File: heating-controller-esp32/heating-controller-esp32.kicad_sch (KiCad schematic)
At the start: 25 parts, among them J3 76829-0104, J4 76829-0104, J5 76829-0104, J6 76829-0104, J7 76829-0104, J8 76829-0104, J9 76829-0104

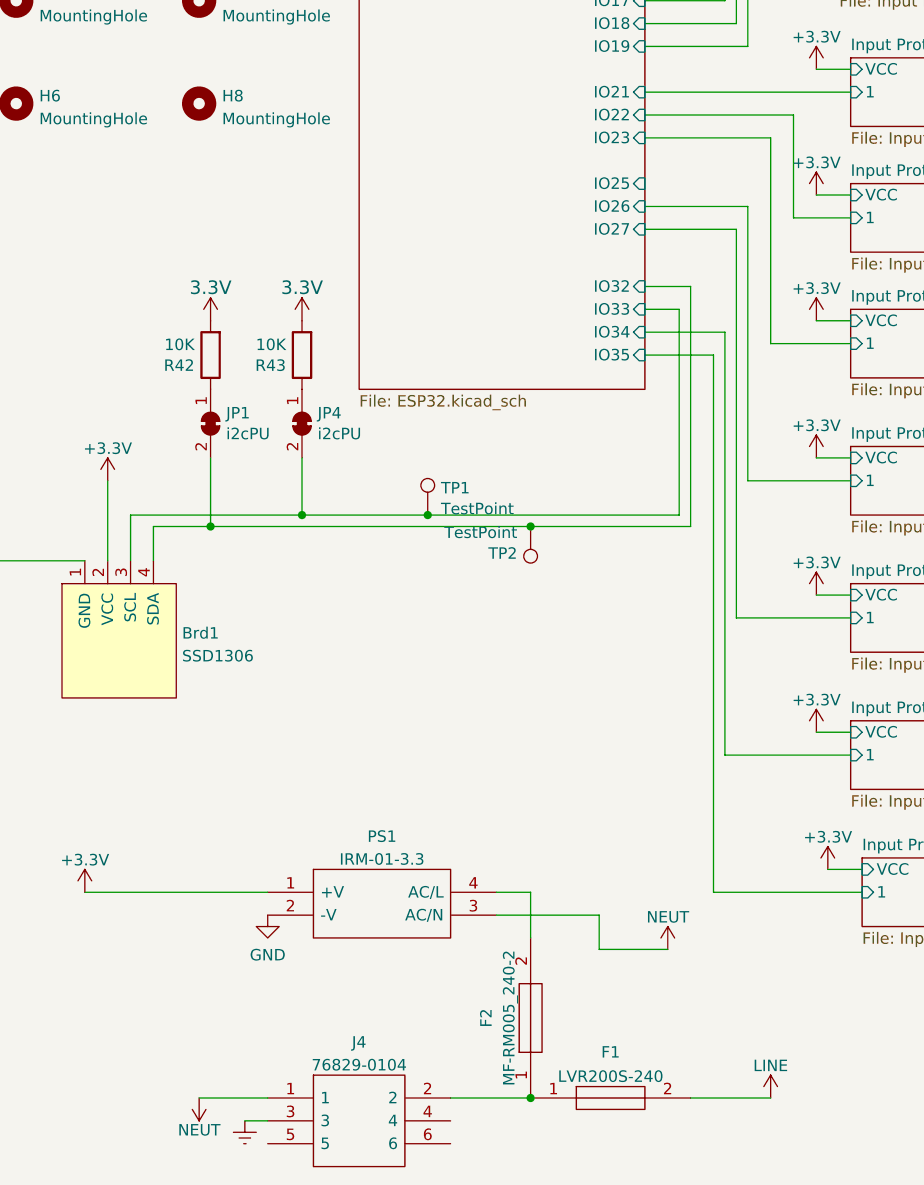
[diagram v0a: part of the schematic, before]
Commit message: Assign netclasses (should have done this earlier)! Small tweaks; status LED added.
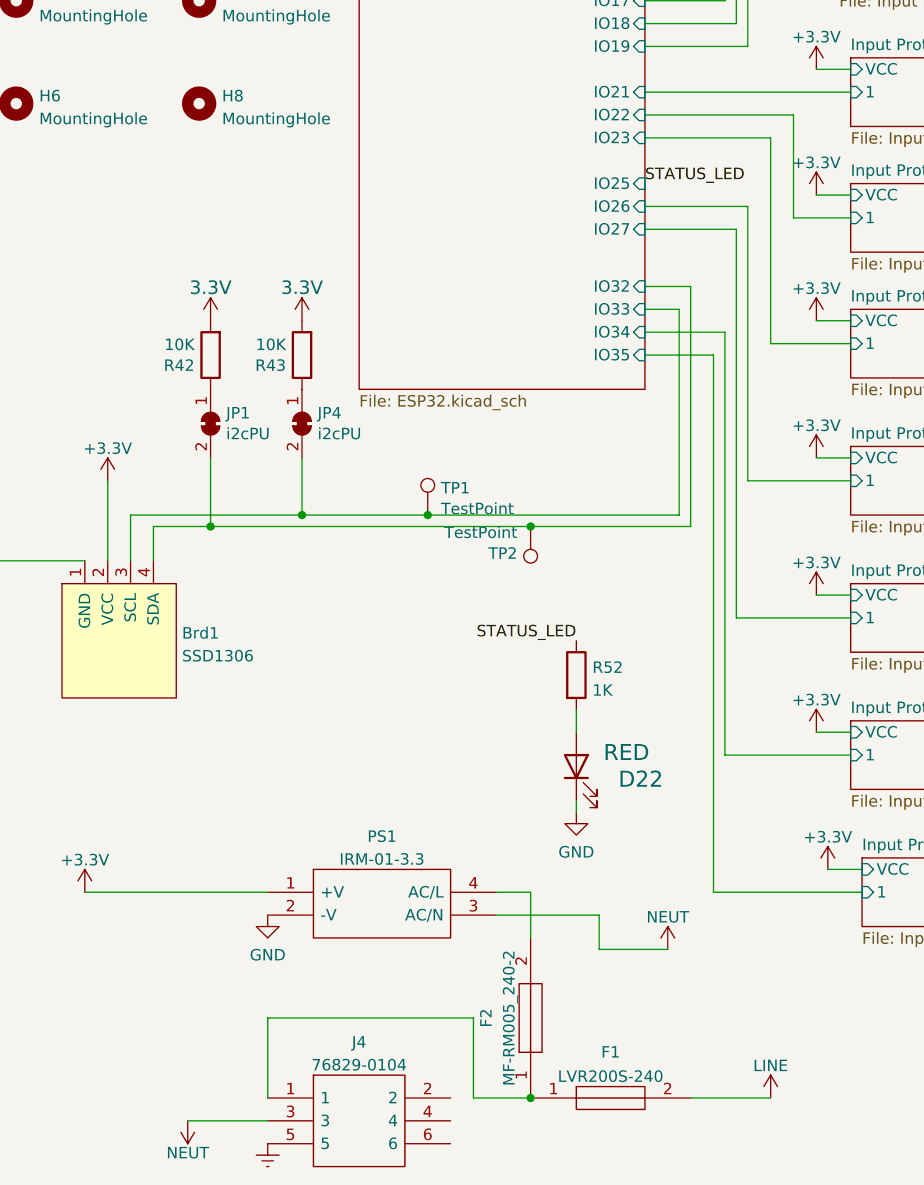
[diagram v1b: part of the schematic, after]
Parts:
- added D22: RED, LED_SMD:LED_0603_1608Metric, symbol Device:LED
- added R52: 1K, Resistor_SMD:R_0603_1608Metric, symbol Device:R
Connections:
- net Earth: now also J4.5; no longer J4.3
- net GND: now also D22.1 (K)
- net NEUT: now also J4.3; no longer J4.1
- net at F1.1, F2.1: now also J4.1; no longer J4.2
- new net: D22.2 (A), R52.2
- new net STATUS_LED: R52.1
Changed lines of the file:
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@@
   (junction (at 77.47 172.72) (diameter 0) (color 0 0 0 0)
   )
-  (wire (pts (xy 68.58 172.72) (xy 77.47 172.72))
-    (stroke (width 0) (type default) (color 0 0 0 0))
-  )
   (wire (pts (xy 100.33 53.34) (xy 100.33 30.48))
     (stroke (width 0) (type default) (color 0 0 0 0))
@@
     (stroke (width 0) (type default) (color 0 0 0 0))
   )
+  (wire (pts (xy 77.47 172.72) (xy 71.12 172.72))
+    (stroke (width 0) (type default) (color 0 0 0 0))
+  )
   (wire (pts (xy 190.5 88.9) (xy 204.47 88.9))
     (stroke (width 0) (type default) (color 0 0 0 0))
@@
     (stroke (width 0) (type default) (color 0 0 0 0))
   )
+  (wire (pts (xy 71.12 163.83) (xy 48.26 163.83))
+    (stroke (width 0) (type default) (color 0 0 0 0))
+  )
   (wire (pts (xy 93.98 15.24) (xy 93.98 40.64))
     (stroke (width 0) (type default) (color 0 0 0 0))
@@
     (stroke (width 0) (type default) (color 0 0 0 0))
   )
-  (wire (pts (xy 48.26 172.72) (xy 40.64 172.72))
-    (stroke (width 0) (type default) (color 0 0 0 0))
-  )
   (wire (pts (xy 100.33 119.38) (xy 113.03 119.38))
     (stroke (width 0) (type default) (color 0 0 0 0))
@@
     (stroke (width 0) (type default) (color 0 0 0 0))
   )
-  (wire (pts (xy 45.72 175.26) (xy 48.26 175.26))
-    (stroke (width 0) (type default) (color 0 0 0 0))
-  )
   (wire (pts (xy 101.6 73.66) (xy 90.17 73.66))
     (stroke (width 0) (type default) (color 0 0 0 0))
@@
     (stroke (width 0) (type default) (color 0 0 0 0))
   )
+  (wire (pts (xy 82.55 139.7) (xy 82.55 140.97))
+    (stroke (width 0) (type default) (color 0 0 0 0))
+  )
   (wire (pts (xy 90.17 45.72) (xy 96.52 45.72))
     (stroke (width 0) (type default) (color 0 0 0 0))
@@
     (stroke (width 0) (type default) (color 0 0 0 0))
   )
+  (wire (pts (xy 82.55 129.54) (xy 82.55 132.08))
+    (stroke (width 0) (type default) (color 0 0 0 0))
+  )
   (wire (pts (xy 101.6 104.14) (xy 101.6 73.66))
     (stroke (width 0) (type default) (color 0 0 0 0))
@@
     (stroke (width 0) (type default) (color 0 0 0 0))
   )
+  (wire (pts (xy 71.12 172.72) (xy 71.12 163.83))
+    (stroke (width 0) (type default) (color 0 0 0 0))
+  )
   (wire (pts (xy 77.47 109.22) (xy 41.91 109.22))
     (stroke (width 0) (type default) (color 0 0 0 0))
@@
     (stroke (width 0) (type default) (color 0 0 0 0))
   )
+  (wire (pts (xy 48.26 163.83) (xy 48.26 172.72))
+    (stroke (width 0) (type default) (color 0 0 0 0))
+  )
   (wire (pts (xy 95.25 109.22) (xy 77.47 109.22))
     (stroke (width 0) (type default) (color 0 0 0 0))
@@
   )
   (wire (pts (xy 85.09 152.4) (xy 85.09 156.21))
+    (stroke (width 0) (type default) (color 0 0 0 0))
+  )
+  (wire (pts (xy 39.37 175.26) (xy 48.26 175.26))
     (stroke (width 0) (type default) (color 0 0 0 0))
   )
@@
     (effects (font (size 1.27 1.27)) (justify left bottom))
   )
+  (label "STATUS_LED" (at 90.17 71.12 0)
+    (effects (font (size 1.27 1.27)) (justify left bottom))
+  )
   (label "Valve_Microswitch_4" (at 137.16 119.38 0)
     (effects (font (size 1.27 1.27)) (justify left bottom))
@@
   (label "Valve_Microswitch_2" (at 226.06 52.07 0)
     (effects (font (size 1.27 1.27)) (justify left bottom))
+  )
+  (label "STATUS_LED" (at 82.55 121.92 180)
+    (effects (font (size 1.27 1.27)) (justify right bottom))
   )
   (label "DHW_Thermostat" (at 232.41 142.24 0)
@@
     (pin "2")
   )
+  (symbol (lib_id "power:GND") (at 82.55 140.97 0) (unit 1)
+    (in_bom yes) (on_board yes) (fields_autoplaced)
+    (property "Reference" "#PWR0192" (id 0) (at 82.55 147.32 0)
+      (effects (font (size 1.27 1.27)) hide)
+    )
+    (property "Value" "GND" (id 1) (at 82.55 145.4134 0))
+    (property "Footprint" "" (id 2) (at 82.55 140.97 0)
+      (effects (font (size 1.27 1.27)) hide)
+    )
+    (property "Datasheet" "" (id 3) (at 82.55 140.97 0)
+      (effects (font (size 1.27 1.27)) hide)
+    )
+    (pin "1")
+  )
   (symbol (lib_id "power:+3.3V") (at 107.95 27.94 0) (unit 1)
     (in_bom yes) (on_board yes) (fields_autoplaced)
@@
     (pin "6")
   )
-  (symbol (lib_id "power:NEUT") (at 40.64 172.72 180) (unit 1)
-    (in_bom yes) (on_board yes) (fields_autoplaced)
-    (property "Reference" "#PWR0115" (id 0) (at 40.64 168.91 0)
-      (effects (font (size 1.27 1.27)) hide)
-    )
-    (property "Value" "NEUT" (id 1) (at 40.64 176.2958 0))
-    (property "Footprint" "" (id 2) (at 40.64 172.72 0)
-      (effects (font (size 1.27 1.27)) hide)
-    )
-    (property "Datasheet" "" (id 3) (at 40.64 172.72 0)
+  (symbol (lib_id "Device:R") (at 82.55 125.73 0) (unit 1)
+    (in_bom yes) (on_board yes) (fields_autoplaced)
+    (property "Reference" "R52" (id 0) (at 84.328 124.8953 0)
+      (effects (font (size 1.27 1.27)) (justify left))
+    )
+    (property "Value" "1K" (id 1) (at 84.328 127.4322 0)
+      (effects (font (size 1.27 1.27)) (justify left))
+    )
+    (property "Footprint" "Resistor_SMD:R_0603_1608Metric" (id 2) (at 80.772 125.73 90)
+      (effects (font (size 1.27 1.27)) hide)
+    )
+    (property "Datasheet" "~" (id 3) (at 82.55 125.73 0)
+      (effects (font (size 1.27 1.27)) hide)
+    )
+    (property "LCSC" "C21190" (id 4) (at 82.55 125.73 0)
+      (effects (font (size 1.27 1.27)) hide)
+    )
+    (pin "1")
+    (pin "2")
+  )
+  (symbol (lib_id "power:NEUT") (at 39.37 175.26 180) (unit 1)
+    (in_bom yes) (on_board yes) (fields_autoplaced)
+    (property "Reference" "#PWR0115" (id 0) (at 39.37 171.45 0)
+      (effects (font (size 1.27 1.27)) hide)
+    )
+    (property "Value" "NEUT" (id 1) (at 39.37 178.8358 0))
+    (property "Footprint" "" (id 2) (at 39.37 175.26 0)
+      (effects (font (size 1.27 1.27)) hide)
+    )
+    (property "Datasheet" "" (id 3) (at 39.37 175.26 0)
       (effects (font (size 1.27 1.27)) hide)
     )
@@
     (pin "6")
   )
-  (symbol (lib_id "power:Earth") (at 45.72 175.26 0) (unit 1)
-    (in_bom yes) (on_board yes) (fields_autoplaced)
-    (property "Reference" "#PWR0116" (id 0) (at 45.72 181.61 0)
-      (effects (font (size 1.27 1.27)) hide)
-    )
-    (property "Value" "Earth" (id 1) (at 45.72 179.07 0)
-      (effects (font (size 1.27 1.27)) hide)
-    )
-    (property "Footprint" "" (id 2) (at 45.72 175.26 0)
-      (effects (font (size 1.27 1.27)) hide)
-    )
-    (property "Datasheet" "~" (id 3) (at 45.72 175.26 0)
+  (symbol (lib_id "power:Earth") (at 48.26 177.8 0) (unit 1)
+    (in_bom yes) (on_board yes) (fields_autoplaced)
+    (property "Reference" "#PWR0116" (id 0) (at 48.26 184.15 0)
+      (effects (font (size 1.27 1.27)) hide)
+    )
+    (property "Value" "Earth" (id 1) (at 48.26 181.61 0)
+      (effects (font (size 1.27 1.27)) hide)
+    )
+    (property "Footprint" "" (id 2) (at 48.26 177.8 0)
+      (effects (font (size 1.27 1.27)) hide)
+    )
+    (property "Datasheet" "~" (id 3) (at 48.26 177.8 0)
       (effects (font (size 1.27 1.27)) hide)
     )
@@
     )
     (pin "1")
+  )
+  (symbol (lib_id "Device:LED") (at 82.55 135.89 90) (unit 1)
+    (in_bom yes) (on_board yes)
+    (property "Reference" "D22" (id 0) (at 92.202 136.271 90)
+      (effects (font (size 1.778 1.778)) (justify left bottom))
+    )
+    (property "Value" "RED" (id 1) (at 90.678 135.382 90)
+      (effects (font (size 1.778 1.778)) (justify left top))
+    )
+    (property "Footprint" "LED_SMD:LED_0603_1608Metric" (id 2) (at 82.55 135.89 0)
+      (effects (font (size 1.27 1.27)) hide)
+    )
+    (property "Datasheet" "" (id 3) (at 82.55 135.89 0)
+      (effects (font (size 1.27 1.27)) hide)
+    )
+    (property "LCSC" "C2286" (id 4) (at 82.55 135.89 90)
+      (effects (font (size 1.27 1.27)) hide)
+    )
+    (pin "1")
+    (pin "2")
   )
   (symbol (lib_id "SamacSys_Parts:MF-RM005_240-2") (at 77.47 172.72 90) (unit 1)
@@
       (reference "#PWR0191") (unit 1) (value "~") (footprint "")
     )
+    (path "/3b711e8c-447f-48ba-b4f0-83160bcd1623"
+      (reference "#PWR0192") (unit 1) (value "GND") (footprint "")
+    )
     (path "/47461e11-6cf0-4201-a11d-7471a93e3671"
       (reference "#SUPPLY0101") (unit 1) (value "3.3V") (footprint "")
@@
       (reference "D21") (unit 1) (value "BAS-040") (footprint "Package_TO_SOT_SMD:SOT-23")
     )
+    (path "/f6469761-311b-4bae-87b6-f2a153492cb8"
+      (reference "D22") (unit 1) (value "RED") (footprint "LED_SMD:LED_0603_1608Metric")
+    )
     (path "/078615e1-25b5-4208-947b-0a8f9b0b55f1"
       (reference "F1") (unit 1) (value "LVR200S-240") (footprint "SamacSys_Parts:LVR200S240")
@@
       (reference "R51") (unit 1) (value "4.7K") (footprint "Resistor_SMD:R_0603_1608Metric")
     )
+    (path "/8ebb9817-9545-4b1e-b218-906da1d224db"
+      (reference "R52") (unit 1) (value "1K") (footprint "Resistor_SMD:R_0603_1608Metric")
+    )
     (path "/28a7b412-fe14-49c0-8d82-0cb1c7505373"
